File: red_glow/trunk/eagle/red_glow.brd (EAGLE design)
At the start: 30.2 x 25.4 mm, 10 parts

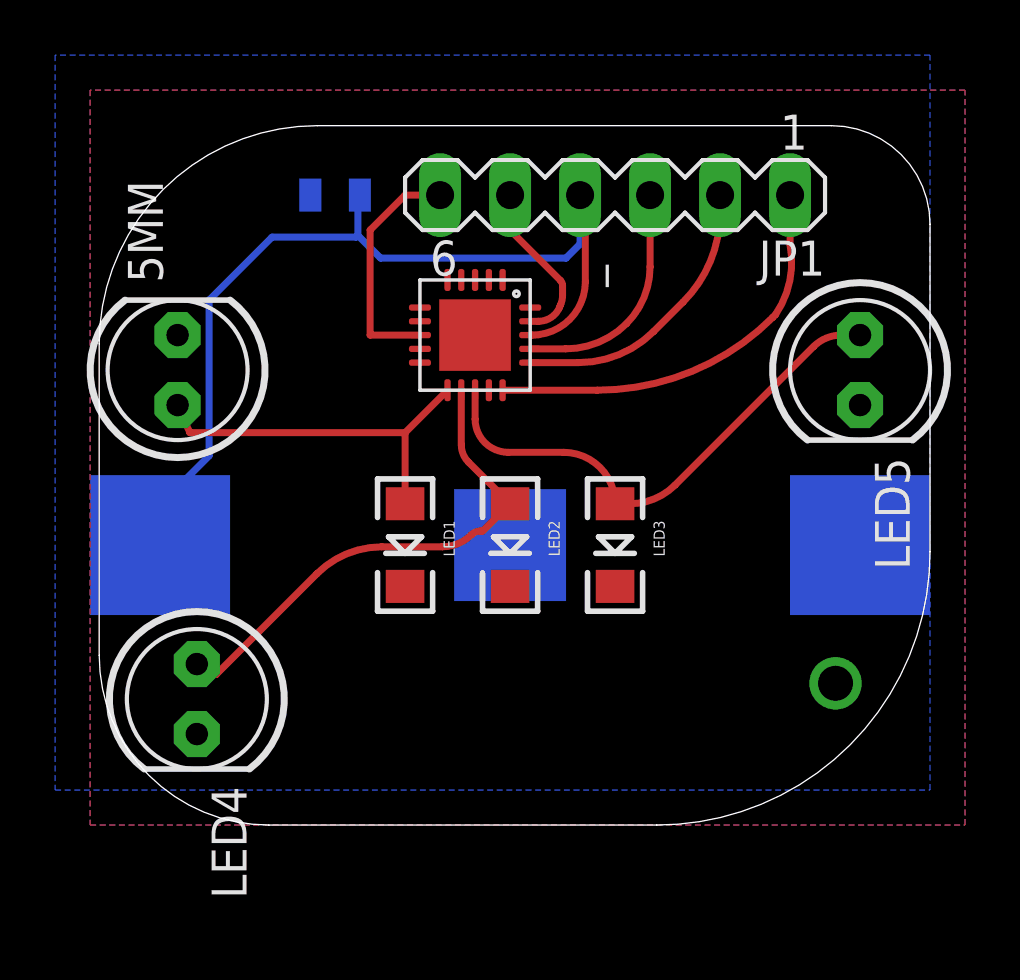
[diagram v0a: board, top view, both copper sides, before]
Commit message: 
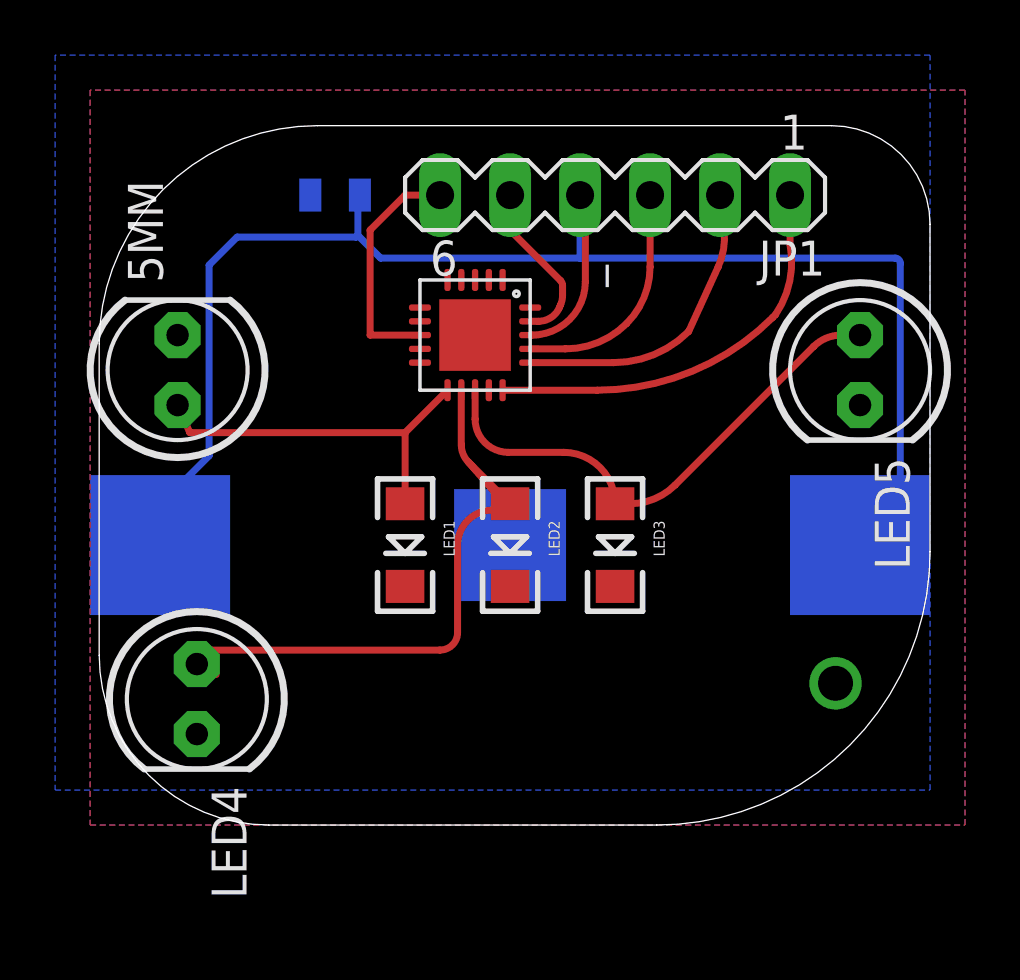
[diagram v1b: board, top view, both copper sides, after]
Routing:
- net VCC: track 33.4 -> 57.0 mm
- net PB2: track 18.5 -> 23.4 mm
- net MISO: track 10.4 -> 11.2 mm
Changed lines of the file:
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@@
 <?xml version="1.0" encoding="utf-8"?>
 <!DOCTYPE eagle SYSTEM "eagle.dtd">
-<eagle version="7.4.0">
+<eagle version="7.6.0">
 <drawing>
 <settings>
@@
 <setting verticaltext="up"/>
 </settings>
-<grid distance="0.05" unitdist="inch" unit="inch" style="lines" multiple="1" display="yes" altdistance="0.0025" altunitdist="inch" altunit="inch"/>
+<grid distance="0.05" unitdist="inch" unit="inch" style="lines" multiple="1" display="yes" altdistance="0.005" altunitdist="inch" altunit="inch"/>
 <layers>
 <layer number="1" name="Top" color="4" fill="1" visible="yes" active="yes"/>
@@
 <contactref element="U$1" pad="+$1"/>
 <contactref element="U$1" pad="+$2"/>
-<wire x1="22.86" y1="48.26" x2="22.86" y2="46.482" width="0.254" layer="16"/>
-<wire x1="22.86" y1="46.482" x2="22.352" y2="45.974" width="0.254" layer="16"/>
-<wire x1="22.352" y1="45.974" x2="15.621" y2="45.974" width="0.254" layer="16"/>
 <wire x1="15.621" y1="45.974" x2="14.7955" y2="46.7995" width="0.254" layer="16"/>
 <wire x1="14.7955" y1="46.7995" x2="14.7955" y2="48.1855" width="0.254" layer="16"/>
@@
 <wire x1="7.62" y1="35.56" x2="7.62" y2="37.0205" width="0.254" layer="16"/>
 <wire x1="7.62" y1="37.0205" x2="9.398" y2="38.7985" width="0.254" layer="16"/>
-<wire x1="9.398" y1="38.7985" x2="9.398" y2="44.45" width="0.254" layer="16"/>
-<wire x1="9.398" y1="44.45" x2="11.684" y2="46.736" width="0.254" layer="16"/>
-<wire x1="11.684" y1="46.736" x2="14.732" y2="46.736" width="0.254" layer="16"/>
+<wire x1="9.398" y1="38.7985" x2="9.398" y2="45.72" width="0.254" layer="16"/>
+<wire x1="9.398" y1="45.72" x2="10.414" y2="46.736" width="0.254" layer="16"/>
+<wire x1="10.414" y1="46.736" x2="14.732" y2="46.736" width="0.254" layer="16"/>
 <wire x1="14.732" y1="46.736" x2="14.7955" y2="46.7995" width="0.254" layer="16"/>
 <wire x1="21.05" y1="43.18" x2="21.115053125" y2="43.18" width="0.254" layer="1"/>
@@
 <wire x1="23.0505" y1="45.115446875" x2="23.0505" y2="47.5615" width="0.254" layer="1"/>
 <wire x1="23.0505" y1="47.5615" x2="22.86" y2="47.752" width="0.254" layer="1"/>
-<wire x1="23.0505" y1="45.115446875" x2="33.02" y2="35.56" width="0" layer="19" extent="1-16"/>
+<wire x1="33.02" y1="35.56" x2="34.4805" y2="37.0205" width="0.254" layer="16"/>
+<wire x1="34.4805" y1="37.0205" x2="34.4805" y2="45.7835" width="0.254" layer="16"/>
+<wire x1="22.86" y1="45.974" x2="34.29" y2="45.974" width="0.254" layer="16"/>
+<wire x1="34.29" y1="45.974" x2="34.4805" y2="45.7835" width="0.254" layer="16" curve="-90"/>
+<wire x1="15.621" y1="45.974" x2="22.86" y2="45.974" width="0.254" layer="16"/>
+<wire x1="22.86" y1="45.974" x2="22.86" y2="48.26" width="0.254" layer="16"/>
 <wire x1="22.86" y1="48.26" x2="22.86" y2="47.752" width="0" layer="19" extent="1-1"/>
 </signal>
@@
 <wire x1="15.24" y1="46.99" x2="16.51" y2="48.26" width="0.254" layer="1"/>
 <wire x1="16.51" y1="48.26" x2="17.78" y2="48.26" width="0.254" layer="1"/>
-<via x="32.131" y="30.5435" extent="1-16" drill="1.27" shape="square"/>
+<via x="32.131" y="30.5435" extent="1-16" drill="1.27"/>
 <polygon width="0.4064" layer="16" isolate="0.254">
 <vertex x="3.81" y="53.34"/>
@@
 <contactref element="_" pad="P$16"/>
 <contactref element="JP1" pad="2"/>
-<wire x1="21.05" y1="42.18" x2="22.80094375" y2="42.18" width="0.254" layer="1"/>
-<wire x1="22.80094375" y1="42.18" x2="25.530703125" y2="43.310703125" width="0.254" layer="1" curve="44.999967"/>
-<wire x1="25.530703125" y1="43.310703125" x2="26.598828125" y2="44.378828125" width="0.254" layer="1"/>
-<wire x1="26.598828125" y1="44.378828125" x2="27.94" y2="47.616703125" width="0.254" layer="1" curve="44.999961"/>
+<wire x1="21.05" y1="42.18" x2="24.07094375" y2="42.18" width="0.254" layer="1"/>
+<wire x1="24.07094375" y1="42.18" x2="26.800703125" y2="43.310703125" width="0.254" layer="1" curve="44.999967"/>
+<wire x1="26.800703125" y1="43.310703125" x2="27.868828125" y2="45.648828125" width="0.254" layer="1"/>
+<wire x1="27.868828125" y1="45.648828125" x2="27.94" y2="47.616703125" width="0.254" layer="1" curve="44.999961"/>
 <wire x1="27.94" y1="47.616703125" x2="27.94" y2="48.26" width="0.254" layer="1"/>
 </signal>
@@
 <contactref element="LED4" pad="A"/>
 <wire x1="8.9535" y1="31.242" x2="9.652" y2="30.861" width="0.254" layer="1"/>
-<wire x1="9.652" y1="30.861" x2="13.312884375" y2="34.521884375" width="0.254" layer="1"/>
-<wire x1="13.312884375" y1="34.521884375" x2="15.6658125" y2="35.4965" width="0.254" layer="1" curve="-45"/>
-<wire x1="15.6658125" y1="35.4965" x2="17.854959375" y2="35.4965" width="0.254" layer="1"/>
-<wire x1="17.854959375" y1="35.4965" x2="18.919409375" y2="35.937409375" width="0.254" layer="1" curve="44.999916"/>
-<wire x1="18.919409375" y1="35.937409375" x2="19.234684375" y2="36.068" width="0.254" layer="1" curve="-45"/>
-<wire x1="19.234684375" y1="36.068" x2="19.328" y2="36.068" width="0.254" layer="1"/>
-<wire x1="19.328" y1="36.068" x2="20.32" y2="37.06" width="0.254" layer="1"/>
+<wire x1="18.810403125" y1="38.569596875" x2="20.32" y2="36.83" width="0.254" layer="1"/>
+<wire x1="20.32" y1="36.83" x2="19.685" y2="36.83" width="0.254" layer="1"/>
+<wire x1="19.685" y1="36.83" x2="18.415" y2="35.56" width="0.254" layer="1" curve="90"/>
+<wire x1="18.415" y1="35.56" x2="18.415" y2="32.385" width="0.254" layer="1"/>
+<wire x1="18.415" y1="32.385" x2="17.78" y2="31.75" width="0.254" layer="1" curve="-90"/>
+<wire x1="17.78" y1="31.75" x2="9.4615" y2="31.75" width="0.254" layer="1"/>
+<wire x1="9.4615" y1="31.75" x2="8.9535" y2="31.242" width="0.254" layer="1" curve="90"/>
 </signal>
 <signal name="PB3">
